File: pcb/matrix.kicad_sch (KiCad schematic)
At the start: 134 parts, among them SW1 ESCAPE, SW10 #9, SW11 #0, SW12 -_, SW13 =+, SW14 BKSPC, SW15 DELETE, SW16 TAB, SW17 Q, SW18 W, SW19 E, SW2 #1, SW20 R, SW21 T, SW22 Y, SW23 U, SW24 I, SW25 O, SW26 P, SW27 [{, SW28 ]}, SW29 \|, SW3 #2, SW30 `~, SW31 CAP, SW32 A, SW33 D, SW34 S, SW35 F, SW36 G, SW37 H, SW38 J, SW39 K, SW4 #3, SW40 L, SW41 ;:, SW42 '", SW43 ENTER, SW44 PGUP, SW45 SHIFT, SW46 Z, SW47 X, SW48 C, SW49 V, SW5 #4, SW50 B, SW51 N, SW52 M, SW53 ,<, SW54 .>, SW55 /?, SW56 SHIFT, SW57 UPROW, SW58 PGDOWN, SW59 CRTL, SW6 #5, SW60 WIN, SW61 ALT, SW62 SPACE, SW63 ALT, SW64 FN, SW65 LEFTROW, SW66 DOWNROW, SW67 RIGHTROW, SW7 #6, SW8 #7, SW9 #8

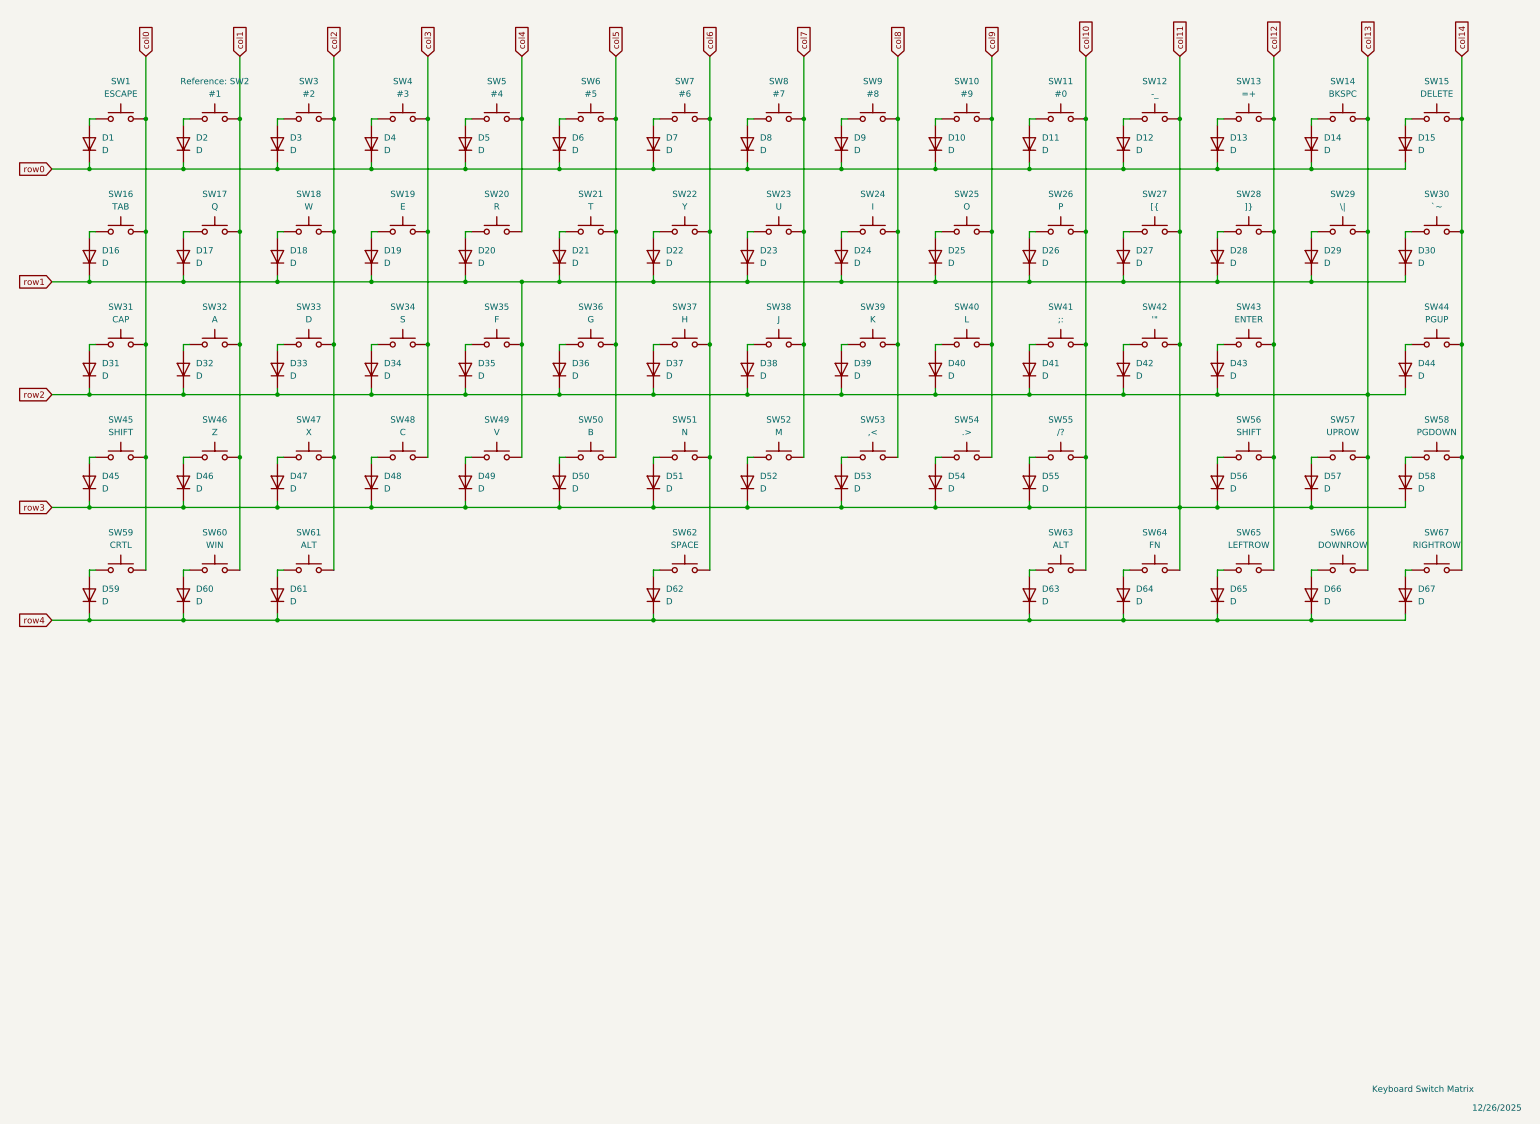
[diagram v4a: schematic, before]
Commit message: Placement of all ICs Finished; Starting Error Checking
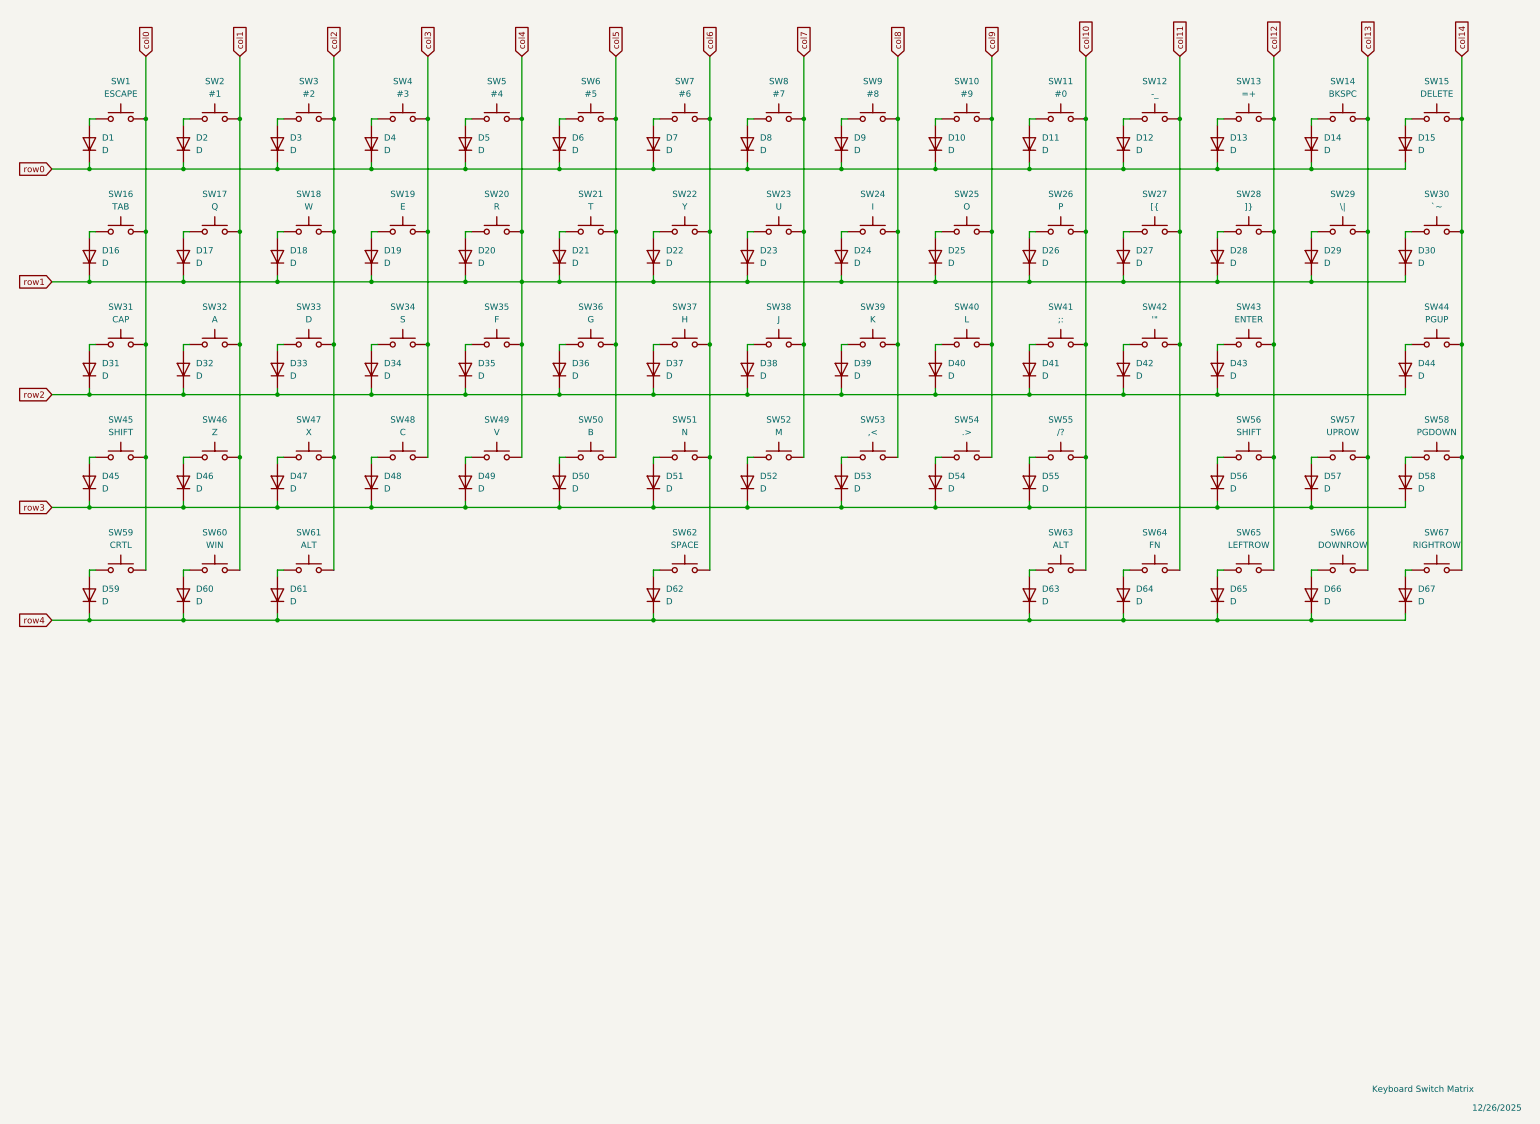
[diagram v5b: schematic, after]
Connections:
- net row1 is gone; now on net col4: D16.1 (K), D17.1 (K), D18.1 (K), D19.1 (K), D20.1 (K), D21.1 (K), D22.1 (K), D23.1 (K), D24.1 (K), D25.1 (K), D26.1 (K), D27.1 (K), D28.1 (K), D29.1 (K), D30.1 (K), SW35.2, SW49.2
- net col11: no longer D45.1 (K), D46.1 (K), D47.1 (K), D48.1 (K), D49.1 (K), D50.1 (K), D51.1 (K), D52.1 (K), D53.1 (K), D54.1 (K), D55.1 (K), D56.1 (K), D57.1 (K), D58.1 (K)
- net col13: no longer D31.1 (K), D32.1 (K), D33.1 (K), D34.1 (K), D35.1 (K), D36.1 (K), D37.1 (K), D38.1 (K), D39.1 (K), D40.1 (K), D41.1 (K), D42.1 (K), D43.1 (K), D44.1 (K)
- new net row2: D31.1 (K), D32.1 (K), D33.1 (K), D34.1 (K), D35.1 (K), D36.1 (K), D37.1 (K), D38.1 (K), D39.1 (K), D40.1 (K), D41.1 (K), D42.1 (K), D43.1 (K), D44.1 (K)
- new net row3: D45.1 (K), D46.1 (K), D47.1 (K), D48.1 (K), D49.1 (K), D50.1 (K), D51.1 (K), D52.1 (K), D53.1 (K), D54.1 (K), D55.1 (K), D56.1 (K), D57.1 (K), D58.1 (K)
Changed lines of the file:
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@@
 	)
 	(junction
-		(at 309.88 135.89)
-		(diameter 0)
-		(color 0 0 0 0)
-	)
-	(junction
 		(at 279.4 135.89)
 		(diameter 0)
@@
 	)
 	(junction
+		(at 138.43 102.87)
+		(diameter 0)
+		(color 0 0 0 0)
+	)
+	(junction
 		(at 62.23 148.59)
 		(diameter 0)
@@
 	)
 	(junction
-		(at 271.78 158.75)
-		(diameter 0)
-		(color 0 0 0 0)
-	)
-	(junction
 		(at 138.43 80.01)
 		(diameter 0)
@@
 	(wire
 		(pts
+			(xy 138.43 102.87) (xy 138.43 113.03)
+		)
+		(stroke
+			(width 0)
+			(type default)
+		)
+	)
+	(wire
+		(pts
 			(xy 298.45 102.87) (xy 298.45 104.14)
 		)
@@
 	(wire
 		(pts
-			(xy 271.78 125.73) (xy 271.78 158.75)
-		)
-		(stroke
-			(width 0)
-			(type default)
-		)
-	)
-	(wire
-		(pts
 			(xy 90.17 102.87) (xy 88.9 102.87)
 		)
@@
 	(wire
 		(pts
-			(xy 309.88 135.89) (xy 317.5 135.89)
-		)
-		(stroke
-			(width 0)
-			(type default)
-		)
-	)
-	(wire
-		(pts
 			(xy 147.32 148.59) (xy 146.05 148.59)
 		)
@@
 	(wire
 		(pts
-			(xy 279.4 135.89) (xy 309.88 135.89)
+			(xy 279.4 135.89) (xy 317.5 135.89)
 		)
 		(stroke
@@
 	(wire
 		(pts
-			(xy 271.78 158.75) (xy 279.4 158.75)
-		)
-		(stroke
-			(width 0)
-			(type default)
-		)
-	)
-	(wire
-		(pts
 			(xy 165.1 158.75) (xy 184.15 158.75)
 		)
@@
 	(wire
 		(pts
-			(xy 241.3 158.75) (xy 271.78 158.75)
+			(xy 241.3 158.75) (xy 279.4 158.75)
 		)
 		(stroke
@@
 	(wire
 		(pts
-			(xy 271.78 158.75) (xy 271.78 171.45)
+			(xy 271.78 125.73) (xy 271.78 171.45)
 		)
 		(stroke
@@
 	(wire
 		(pts
-			(xy 309.88 102.87) (xy 309.88 135.89)
+			(xy 309.88 102.87) (xy 309.88 148.59)
 		)
 		(stroke
@@
 	(wire
 		(pts
-			(xy 309.88 135.89) (xy 309.88 148.59)
-		)
-		(stroke
-			(width 0)
-			(type default)
-		)
-	)
-	(wire
-		(pts
 			(xy 50.8 180.34) (xy 50.8 181.61)
 		)
@@
 		(property "Reference" "SW2"
 			(at 76.2 72.39 0)
-			(show_name yes)
 			(effects
 				(font
